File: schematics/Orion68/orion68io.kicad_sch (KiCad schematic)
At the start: 32 parts, among them J200 Euro96pin, U200 GAL16V8

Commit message: RTC rcp5c01A working...
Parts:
- removed J_S100: DB25_Socket, Connector_PinHeader_2.54mm:PinHeader_2x13_P2.54mm_Vertical, symbol Connector:DB25_Socket
- removed J_S201: RTC, Connector_PinSocket_2.54mm:PinSocket_1x06_P2.54mm_Vertical, symbol Connector_Generic:Conn_01x06
- removed R200, R201, R202, R203, R204, R205, R206, R207, R208, R209, R210, R211, R212: 1k, Resistor_THT:R_Axial_DIN0204_L3.6mm_D1.6mm_P5.08mm_Horizontal, symbol Device:R
- removed R213, R214: 4k7, Resistor_THT:R_Axial_DIN0204_L3.6mm_D1.6mm_P5.08mm_Horizontal, symbol Device:R
- removed U_S100: 82C55A, Package_DIP:DIP-40_W15.24mm, symbol Interface:82C55A
- removed U_S201, U_S202: 74HC245, Package_DIP:DIP-20_W7.62mm, symbol 74xx:74HC245
- added BT1: Battery, symbol Device:Battery
- added C1, C14: 100nF, symbol Device:C
- added C10: 4,7uF, symbol Device:C_Polarized
- added C11: 6,8pF a 45pF, symbol Device:C_Trim
- added C12: 56pF, symbol Device:C
- added C13: 22pF, symbol Device:C
- added C15: 100uF, symbol Device:C_Polarized
- added D6, D8: 1N5819, Diode_SMD:D_SOD-523, symbol Diode:1N4148WT
- added J1: LevelConverter, symbol Connector_Generic:Conn_02x06_Odd_Even
- added JP1, JP2: Conn_02x12_Odd_Even, symbol Connector_Generic:Conn_02x12_Odd_Even
- added R17: 1k2, symbol Device:R
- added R18: 100k, symbol Device:R
- added R55: 10k, symbol Device:R
- added U25, U26: SN74LVC245APW, Package_SO:TSSOP-20_4.4x6.5mm_P0.65mm, symbol Logic_LevelTranslator:SN74LVC245APW
- added U27: RP5C01A, symbol pdSilva:RP5C01A
- added U30: LM2937xT, Package_TO_SOT_THT:TO-220-3_Vertical, symbol Regulator_Linear:LM2937xT
- added Y3: Crystal, symbol Device:Crystal
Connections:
- net 3V3_from_sdcard is gone; now on net 3V3: U_S200.39 (VSYS)
- net BA08 is gone; now on net A10: U200.3 (I3)
- net BA09 is gone; now on net A11: U200.4 (I4)
- net BA10 is gone; now on net A12: U200.5 (I5)
- net BA11 is gone; now on net A13: U200.6 (I6)
- net /BAS is gone; now on net A14: U200.7 (I7)
- net /BLDS is gone; now on net A15: U200.8 (I8)
- net /BUDS is gone; now on net /IO_CS: U200.9 (I9)
- net +5V: now also C14.1, D8.2 (A), R55.2, U30.1 (VI); no longer J_S200.2 (Pin_2)
- net A1: now also JP1.22 (Pin_22), U26.18 (B1), U27.4 (A0)
- net A10: now also JP1.11 (Pin_11)
- net A11: now also JP1.12 (Pin_12)
- net A12: now also JP1.9 (Pin_9)
- net A13: now also JP1.10 (Pin_10)
- net A14: now also JP1.7 (Pin_7)
- net A2: now also JP1.21 (Pin_21), U26.17 (B2), U27.5 (A1)
- net A3: now also JP1.20 (Pin_20), U26.16 (B3), U27.6 (A2)
- net A4: now also JP1.19 (Pin_19), U26.15 (B4), U27.7 (A3)
- net A5: now also JP1.18 (Pin_18)
- net A6: now also JP1.17 (Pin_17)
- net A7: now also JP1.16 (Pin_16)
- net A8: now also JP1.15 (Pin_15)
- net A9: now also JP1.14 (Pin_14)
- net B/cpurd: no longer U200.12 (IO8)
- net B/cpurw: no longer U200.13 (IO7)
- net CS: no longer U_S200.22 (GP17)
- net D0: now also JP2.16 (Pin_16), U25.18 (B1), U27.11 (D0)
- net D1: now also JP2.15 (Pin_15), U25.17 (B2), U27.12 (D1)
- net D2: now also JP2.18 (Pin_18), U25.16 (B3), U27.13 (D2)
- net D3: now also JP2.17 (Pin_17), U25.15 (B4), U27.14 (D3)
- net D4: now also JP2.20 (Pin_20), U25.14 (B5)
- net D5: now also JP2.19 (Pin_19), U25.13 (B6)
- net D6: now also JP2.22 (Pin_22), U25.12 (B7)
- net D7: now also JP2.21 (Pin_21), U25.11 (B8)
- net GND: now also BT1.2 (-), C1.2, C10.2, C11.2, C12.2, C13.2, C14.2, C15.2, J1.5 (Pin_5), J1.6 (Pin_6), JP1.13 (Pin_13), JP1.24 (Pin_24), JP1.8 (Pin_8), JP2.1 (Pin_1), JP2.13 (Pin_13), JP2.14 (Pin_14), JP2.23 (Pin_23), JP2.4 (Pin_4), JP2.7 (Pin_7), U25.10 (GND), U26.1 (DIR), U26.10 (GND), U26.19 (~{OE}), U27.3 (ADJ), U27.9 (GND), U30.2 (GND)
- net MISO: no longer U_S200.21 (GP16)
- net MOSI: no longer U_S200.25 (GP19)
- net SCK: no longer U_S200.24 (GP18)
- net audio: no longer U_S200.29 (GP22)
- net /AS: now also U200.12 (IO8)
- net /CS_IDE: no longer U200.18 (IO2)
- net /CS_MULTIO: now also U200.18 (IO2), U25.19 (~{OE}), U26.13 (B6); no longer U200.15 (IO5), U_S200.26 (GP20)
- net /CS_RTC: now also U27.1 (/CS)
- net /IO_CS: no longer U200.11 (I10/~{OE})
- net /IO_CS1: now also U200.11 (I10/~{OE})
- net /RD: now also JP1.4 (Pin_4), U27.8 (/RD); no longer U_S200.17 (GP13)
- net /RESET: now also JP2.2 (Pin_2)
- net /WR: now also JP1.3 (Pin_3), U25.1 (DIR), U26.14 (B5), U27.10 (/WR); no longer U_S200.16 (GP12)
- net at U_S200.1 (GP0): now also U25.2 (A1)
- net at U_S200.10 (GP7): now also U25.9 (A8)
- net A1_C: now reaches U_S200.11 (GP8)
- net A1_C: now also U26.2 (A1)
- net A2_C: now reaches U_S200.12 (GP9)
- net A2_C: now also U26.3 (A2)
- net A3_C: now reaches U_S200.14 (GP10)
- net A3_C: now also U26.4 (A3)
- net A4_C: now reaches U_S200.15 (GP11)
- net A4_C: now also U26.5 (A4)
- net RX: now reaches U_S200.19 (GP14)
- net RX: now also J1.10 (Pin_10)
- net at U_S200.2 (GP1): now also U25.3 (A2)
- net /CS_MULTIO_C: now reaches U_S200.20 (GP15)
- net /CS_MULTIO_C: now also U26.7 (A6)
- net CS_WIZNET: now reaches U_S200.27 (GP21)
- net 3V3: now reaches U_S200.39 (VSYS)
- net 3V3: now also J_S200.2 (Pin_2), C15.1, U25.20 (VCC), U26.20 (VCC), U30.3 (VO)
- net at U_S200.4 (GP2): now also U25.4 (A3)
- net at U_S200.5 (GP3): now also U25.5 (A4)
- net at U_S200.6 (GP4): now also U25.6 (A5)
- net at U_S200.7 (GP5): now also U25.7 (A6)
- net at U_S200.9 (GP6): now also U25.8 (A7)
- net BA06 renamed A08
- net BA07 renamed A09
- net IRQ3 renamed HV4
- net HV4: now also J1.11 (Pin_11)
- net SCL renamed Audio
- net SDA renamed MOSI_SPI1
- net TICK_IN renamed /DTACK_RPI
- net /DTACK_RPI: now also J1.2 (Pin_2)
- net /CS_82C55 renamed CS_KBD
- net /CS_SDCARD: no longer names the net of U200.14 (IO6)
- net /CS_TIMER: no longer names the net of U200.16 (IO4)
- new net: C11.1, C12.1, U27.16 (OSCIN), Y3.1
- new net: C1.1, C10.1, D6.1 (K), D8.1 (K), U27.18 (VCC), U27.2 (CS)
- new net: C13.1, R18.1, Y3.2
- new net: R55.1, U27.15 (/ALRM)
- new net: R18.2, U27.17 (OSCOUT)
- new net: D6.2 (A), R17.2
- new net: BT1.1 (+), R17.1
- new net 3,3V: J1.8 (Pin_8)
- new net 5V: J1.7 (Pin_7)
- new net A0: JP1.23 (Pin_23)
- new net COL_LED: JP2.6 (Pin_6)
- new net CS_SDCARD: U_S200.22 (GP17)
- new net FDX_LED: JP2.11 (Pin_11)
- new net HV1: J1.1 (Pin_1)
- new net INT: J1.12 (Pin_12)
- new net LINK_LED: JP2.12 (Pin_12)
- new net MISO_SPI0: U_S200.21 (GP16)
- new net MISO_SPI1: U_S200.26 (GP20)
- new net MOSI_SPI0: U_S200.25 (GP19)
- new net NC: JP1.6 (Pin_6), JP2.3 (Pin_3), JP2.5 (Pin_5), JP2.9 (Pin_9)
- new net RX_LED: JP2.10 (Pin_10)
- new net RX_OUT: J1.9 (Pin_9)
- new net SCK_SPI0: U_S200.24 (GP18)
- new net SCK_SPI1: U_S200.29 (GP22)
- new net TX: J1.4 (Pin_4), U_S200.17 (GP13)
- new net TX_LED: JP2.8 (Pin_8)
- new net TX_OUT: J1.3 (Pin_3)
- new net VCC_3V3: JP1.1 (Pin_1), JP2.24 (Pin_24)
- new net /CS: JP1.5 (Pin_5)
- new net /INT: JP1.2 (Pin_2)
- new net /WR_C: U26.6 (A5), U_S200.16 (GP12)
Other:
- note added: "FF9000->Keyboard PS2 FF9100->Super MultiIO FF9200->RTC RP5C01A da Ricoh"
- note added: "Modulo Wiznet W5100"
- note added: "Setor S100A"
- note added: "Setor S100B"
- note added: "Setor S300"
- note added: "dir = 1 A -> B dir = 0 B -> A"
- note removed: "+---------+-----+---------+------------+ |Binário | LDS | Ender. |D0-D7 (LDS)| |A5...A1 | A0 | Decimal |D8-D15 (UDS)| +---------+-----+---------+------------+ |00000 | 0 | 0(Par) | LDS | |00000 | 1 | 1(Ímpar)| UDS | |00001 | 0 | 2(Par) | LDS | |00001 | 1 | 3(Ímpar)| UDS | |00010 | 0 | 4(Par) | LDS | |00010 | 1 | 5(Ímpar)| UDS | |00011 | 0 | 6(Par) | LDS | |00011 | 1 | 7(Ímpar)| UDS | |00100 | 0 |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"
- note removed: "0xF00040-0xF0007F -> 82C55 0xF00080-0xF000BF -> IDE 0xF000C0-0xF000FF -> RTC 0xF00140-0xF0017F -> TIMER 0xF00180-0xF001BF -> SDCARD 0xF001C0-0xF001FF -> free 0xF00240-0xF0027F -> free 0xF00280-0xF002BF -> free 0xF002C0-0xF002FF -> free 0xF00340-0xF0037F -> free 0xFB8000-0xFB803F -> VGA-CARD"
- note removed: "DB25 fêmea +-------+--------------+--------------+---------------------------------------------+ |Pino |,Nome |,Direção (PC) |,Função | +-------+--------------+--------------+---------------------------------------------+ |1 |,Strobe |,Saída |,Indica que os dados são válidos (Ativo em 0)| |2 |,D0 |,E/S |,Bit de Dados 0 (LSB) | |3 |,D1 |,E/S |,Bit de Dados 1 | |4 |,D2 |,E/S |,Bit de Dados 2 | |5 |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"
- moved on the sheet: D_S500, J200, J_S200, J_S500, R_S500

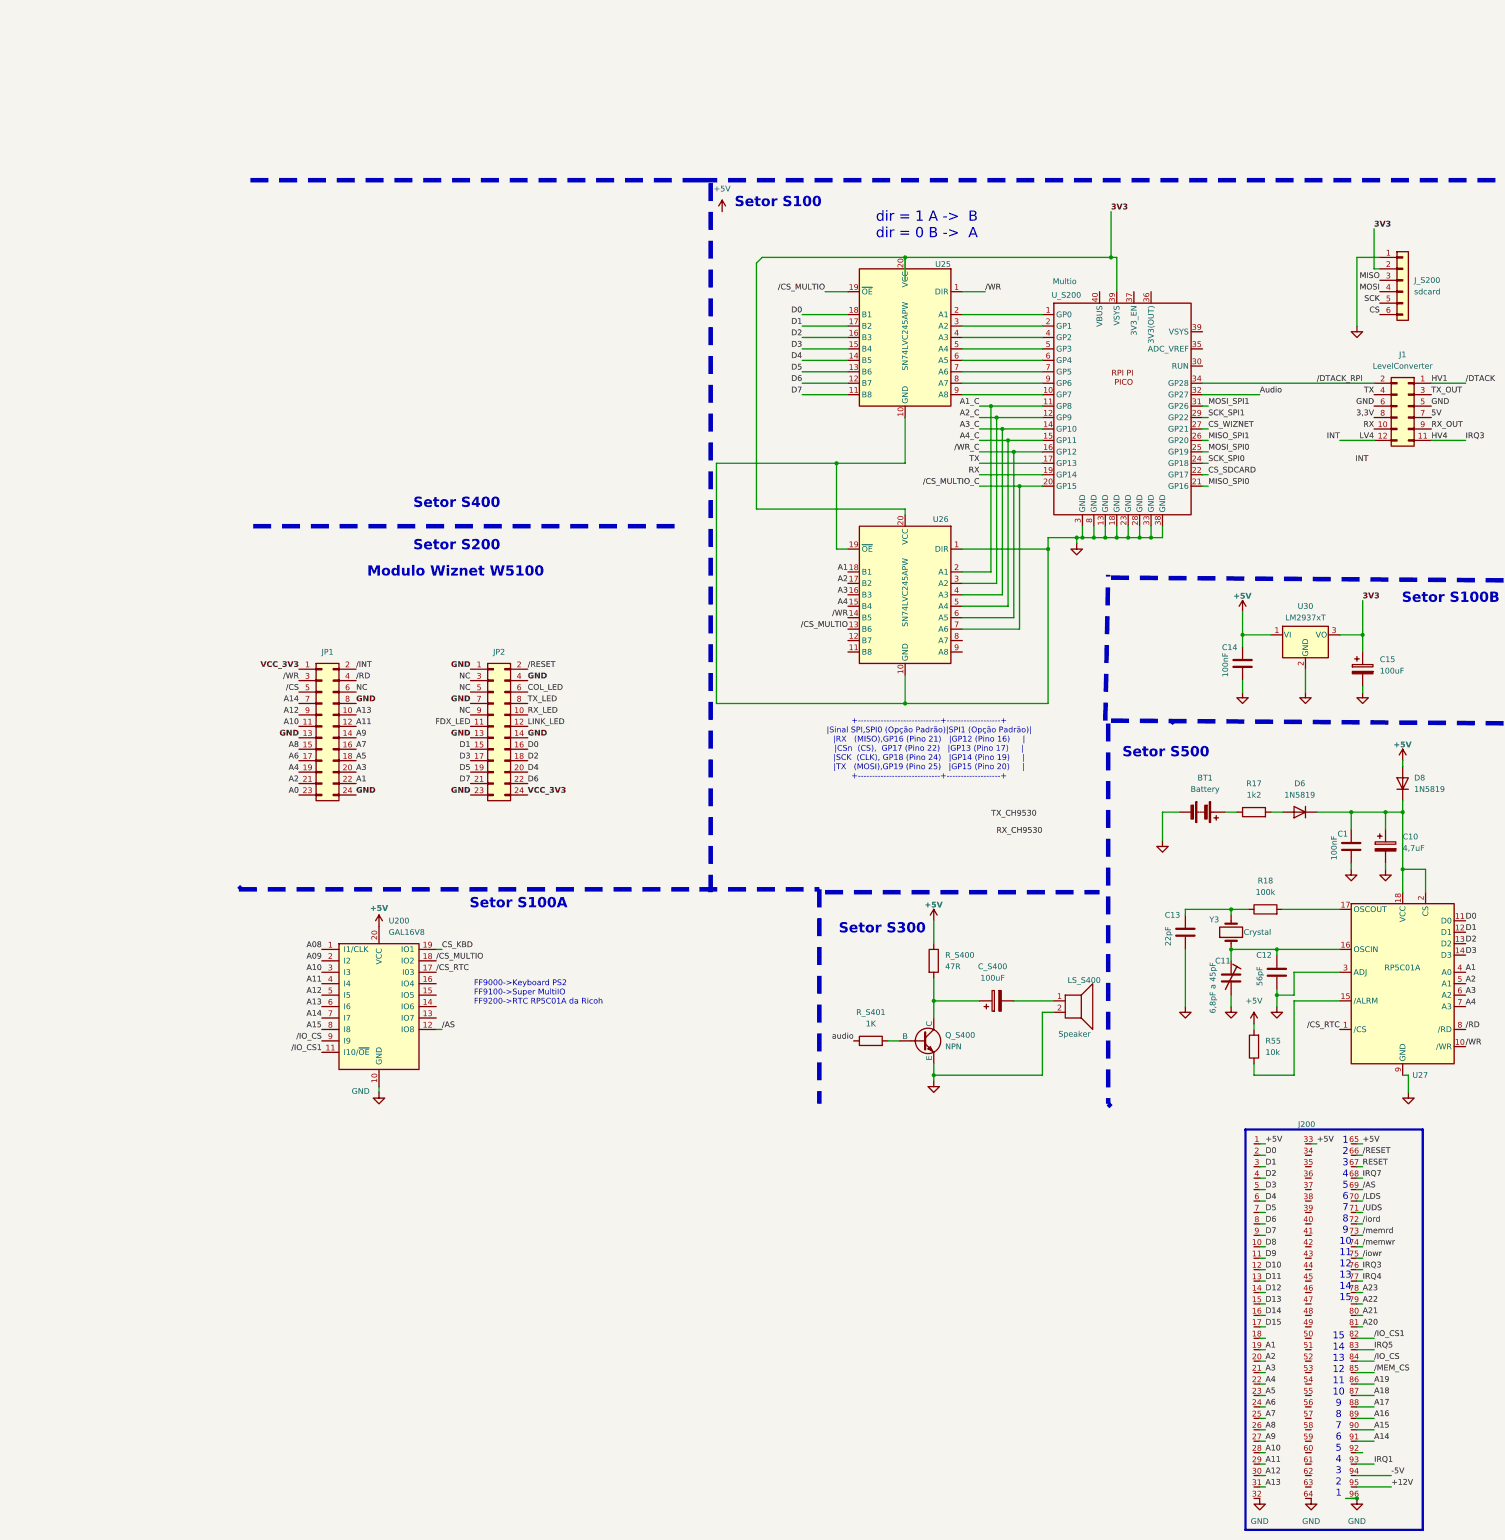
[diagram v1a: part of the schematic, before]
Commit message: First test with picow for ethernet
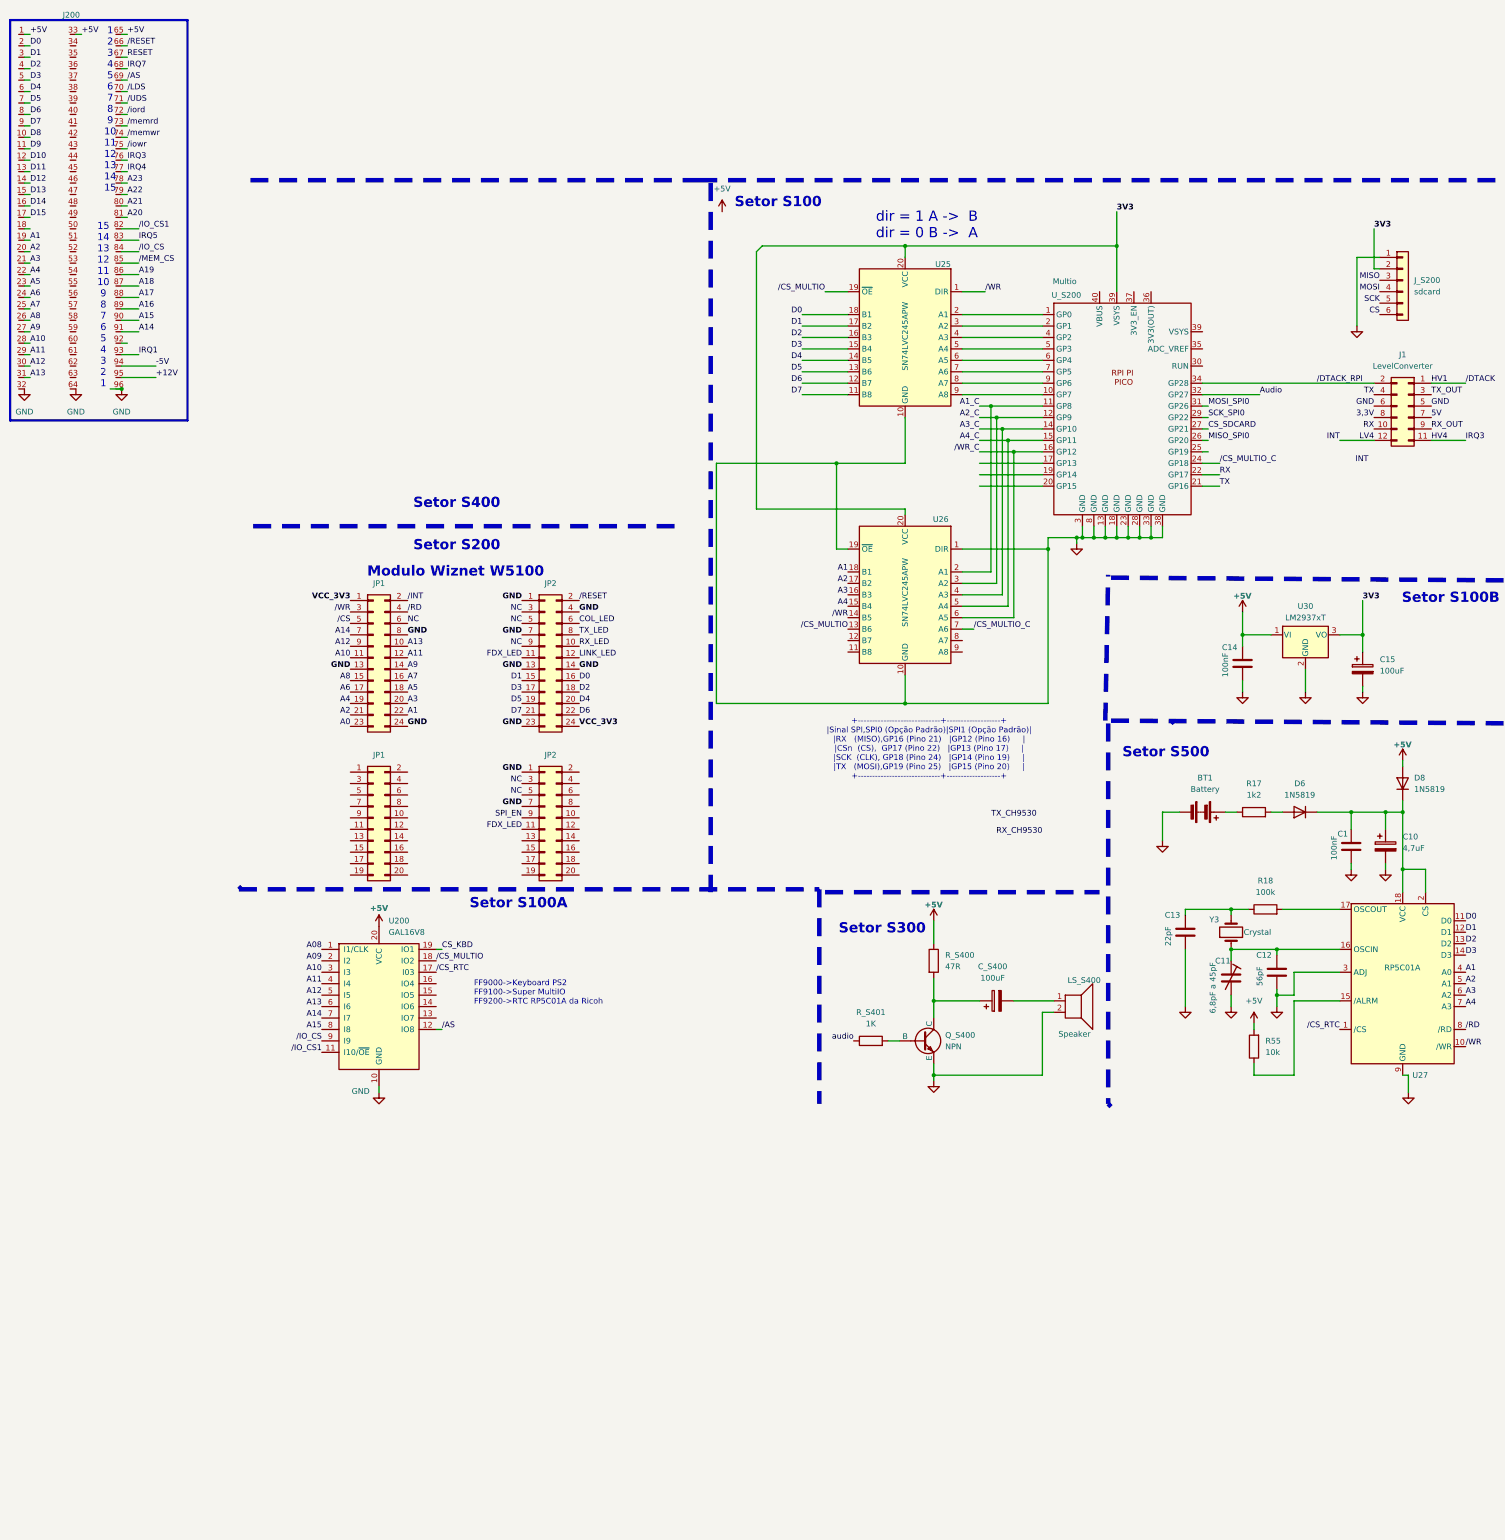
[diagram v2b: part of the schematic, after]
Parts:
- added JP1, JP2: Conn_02x10_Odd_Even, symbol Connector_Generic:Conn_02x10_Odd_Even
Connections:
- net CS_WIZNET is gone; now on net CS_SDCARD: U_S200.27 (GP21)
- net MISO_SPI1 is gone; now on net MISO_SPI0: U_S200.26 (GP20)
- net MOSI_SPI1 is gone; now on net MOSI_SPI0: U_S200.31 (GP26)
- net SCK_SPI1 is gone; now on net SCK_SPI0: U_S200.29 (GP22)
- net CS_SDCARD: no longer U_S200.22 (GP17)
- net FDX_LED: now also JP2.11 (Pin_11)
- net GND: now also JP2.1 (Pin_1), JP2.7 (Pin_7)
- net MISO_SPI0: no longer U_S200.21 (GP16)
- net MOSI_SPI0: no longer U_S200.25 (GP19)
- net NC: now also JP2.3 (Pin_3), JP2.5 (Pin_5)
- net RX: now also U_S200.22 (GP17); no longer U_S200.19 (GP14)
- net SCK_SPI0: no longer U_S200.24 (GP18)
- net TX: now also U_S200.21 (GP16); no longer U_S200.17 (GP13)
- net /CS_MULTIO_C: now also U_S200.24 (GP18); no longer U_S200.20 (GP15)
- new net SPI_EN: JP2.9 (Pin_9)
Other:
- moved on the sheet: J200, JP1, JP2

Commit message: Ps2 keyboard running...
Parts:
- added PS/1: Mini-DIN-6, JJ65c02:mini_din-6, symbol Connector:Mini-DIN-6
- added R_S1, R_S2: 4k7, Resistor_THT:R_Axial_DIN0204_L3.6mm_D1.6mm_P5.08mm_Horizontal, symbol Device:R
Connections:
- net 3V3: now also R_S1.2, R_S2.2
- net A5: now also U26.12 (B7)
- net A6: now also U26.11 (B8)
- net GND: now also PS/1.3
- net HV4: now also U_S200.25 (GP19)
- net RX: no longer U_S200.22 (GP17)
- net TX: no longer U_S200.21 (GP16)
- net /WR_C: now also U_S200.20 (GP15); no longer U_S200.16 (GP12)
- net A6_C: now reaches U_S200.17 (GP13)
- net A6_C: now also U26.9 (A8)
- net A5_C: now reaches U26.8 (A7)
- net A5_C: now also U_S200.16 (GP12)
- new net +5v: PS/1.4
- new net PS2_CLK: PS/1.5, R_S1.1, U_S200.22 (GP17)
- new net PS2_DATA: PS/1.1, R_S2.1, U_S200.21 (GP16)
- no-connect marks 6 -> 8
